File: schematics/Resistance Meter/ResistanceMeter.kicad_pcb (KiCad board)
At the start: 2 copper layers, 52.7 x 54.6 mm, 29 parts, among them J1 Conn_01x01_Female, J2 Conn_01x01_Female, J3 Conn_01x16_Female, J4 Conn_01x08_Male, J5 Conn_01x06_Male, J6 Conn_01x10_Male, J7 Conn_01x08_Male, Q1 IRF540N, Q2 IRF540N, SW1 SW_Push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

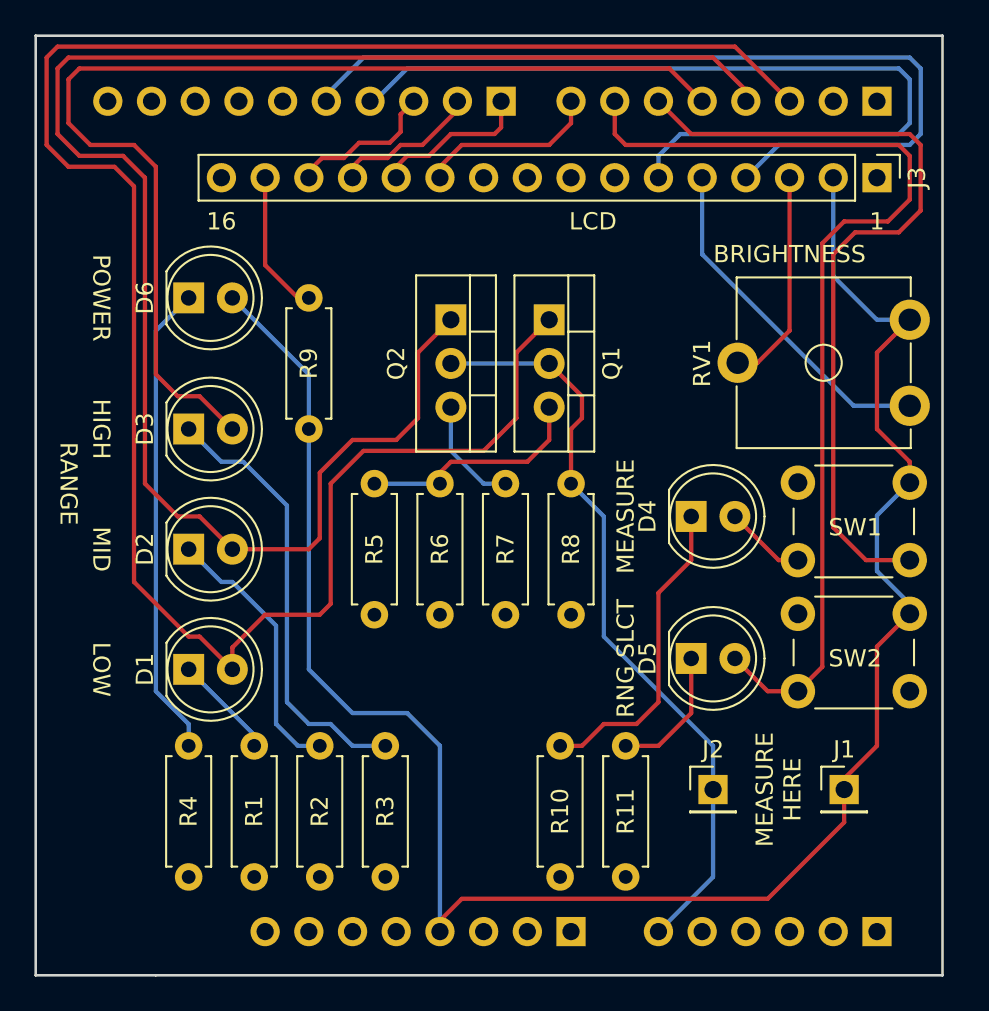
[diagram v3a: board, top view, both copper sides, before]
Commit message: Update to KiCad 5 from 4
- use KiCad's standard library Arduino shield symbol and footprint
- ground the second copper layer of the PCB (and consequently unground
the first copper layer of the PCB)
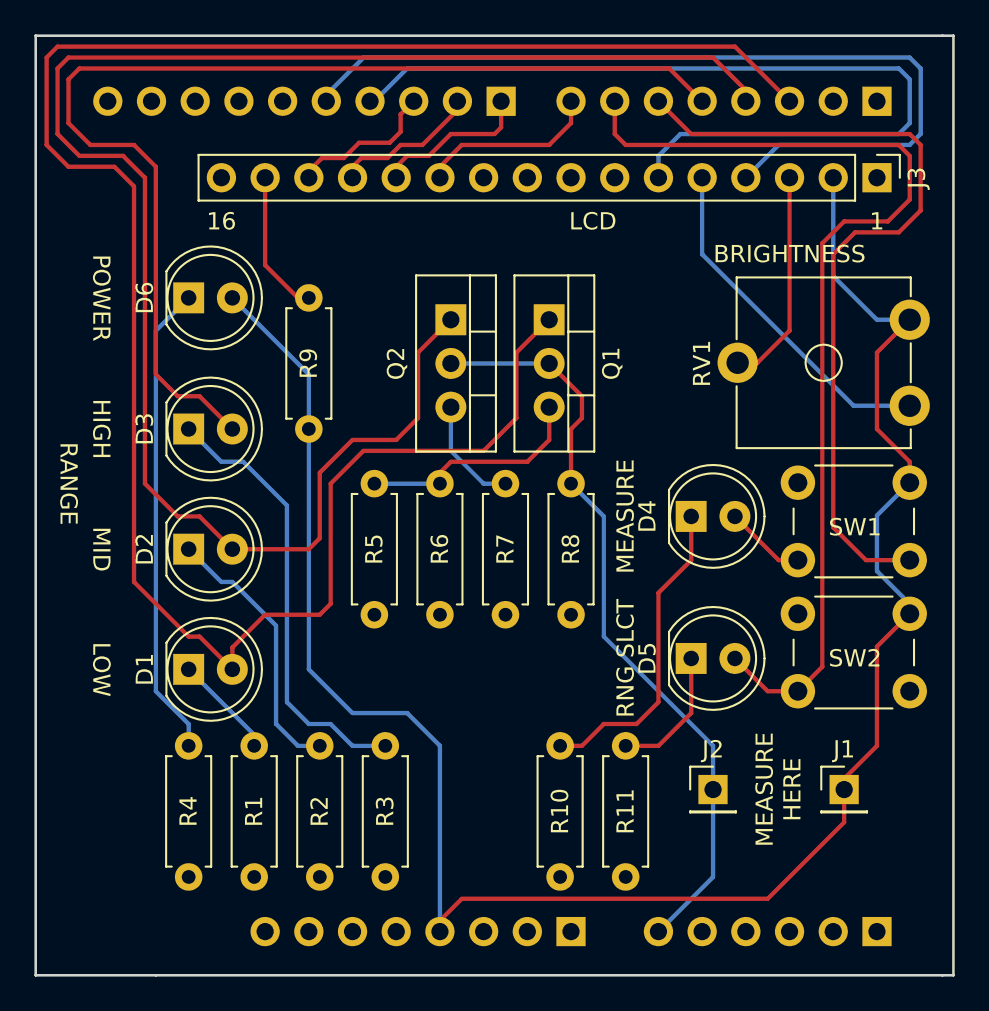
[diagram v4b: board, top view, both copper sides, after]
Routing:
- added copper zone on B.Cu, net Earth
- removed copper zone on F.Cu, net Earth
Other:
- board size 52.7 x 54.6 mm -> 53.3 x 54.6 mm
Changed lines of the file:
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@@
-(kicad_pcb (version 4) (host pcbnew 4.0.7-e2-6376~61~ubuntu18.04.1)
+(kicad_pcb (version 20171130) (host pcbnew 5.0.0-fee4fd1~65~ubuntu18.04.1)
   (general
-    (links 55)
-    (no_connects 4)
-    (area 128.194999 64.694999 181.050001 119.455001)
     (thickness 1.6)
-    (drawings 18)
+    (drawings 20)
     (tracks 207)
     (zones 0)
@@
     (visible_elements FFFFFF7F)
     (pcbplotparams
-      (layerselection 0x00030_80000001)
+      (layerselection 0x010f0_ffffffff)
       (usegerberextensions false)
+      (usegerberattributes false)
+      (usegerberadvancedattributes false)
+      (creategerberjobfile false)
       (excludeedgelayer true)
       (linewidth 0.100000)
@@
       (hpglpennumber 1)
       (hpglpenspeed 20)
-      (hpglpendiameter 15)
-      (hpglpenoverlay 2)
+      (hpglpendiameter 15.000000)
       (psnegative false)
       (psa4output false)
@@
       (outputformat 1)
       (mirror false)
-      (drillshape 1)
+      (drillshape 0)
       (scaleselection 1)
-      (outputdirectory ""))
+      (outputdirectory "gerber/"))
   )
   (net 0 "")
@@
       (net 45 "Net-(Q1-Pad3)"))
     (model ${KISYS3DMOD}/TO_SOT_Packages_THT.3dshapes/TO-220-3_Vertical.wrl
-      (at (xyz 0.1 0 0))
+      (offset (xyz 2.539999961853027 0 0))
       (scale (xyz 0.393701 0.393701 0.393701))
       (rotate (xyz 0 0 0))
@@
       (net 2 Earth))
     (model ${KISYS3DMOD}/Socket_Strips.3dshapes/Socket_Strip_Straight_1x16_Pitch2.54mm.wrl
-      (at (xyz 0 -0.75 0))
+      (offset (xyz 0 -19.04999971389771 0))
       (scale (xyz 1 1 1))
       (rotate (xyz 0 0 270))
@@
     (fp_line (start 1.8 -19.55) (end 1.8 1.8) (layer B.CrtYd) (width 0.05))
     (fp_line (start 1.8 1.8) (end -1.8 1.8) (layer B.CrtYd) (width 0.05))
-    (fp_text user %R (at 0 -8.89 360) (layer B.Fab)
+    (fp_text user %R (at 0 -8.89) (layer B.Fab)
       (effects (font (size 1 1) (thickness 0.15)) (justify mirror))
     )
@@
     (fp_line (start 1.8 -14.5) (end 1.8 1.8) (layer B.CrtYd) (width 0.05))
     (fp_line (start 1.8 1.8) (end -1.8 1.8) (layer B.CrtYd) (width 0.05))
-    (fp_text user %R (at 0 -6.35 360) (layer B.Fab)
+    (fp_text user %R (at 0 -6.35) (layer B.Fab)
       (effects (font (size 1 1) (thickness 0.15)) (justify mirror))
     )
@@
     (fp_line (start 1.8 -24.65) (end 1.8 1.8) (layer B.CrtYd) (width 0.05))
     (fp_line (start 1.8 1.8) (end -1.8 1.8) (layer B.CrtYd) (width 0.05))
-    (fp_text user %R (at 0 -11.43 360) (layer B.Fab)
+    (fp_text user %R (at 0 -11.43) (layer B.Fab)
       (effects (font (size 1 1) (thickness 0.15)) (justify mirror))
     )
@@
     (fp_line (start 1.8 -19.55) (end 1.8 1.8) (layer B.CrtYd) (width 0.05))
     (fp_line (start 1.8 1.8) (end -1.8 1.8) (layer B.CrtYd) (width 0.05))
-    (fp_text user %R (at 0 -8.89 360) (layer B.Fab)
+    (fp_text user %R (at 0 -8.89) (layer B.Fab)
       (effects (font (size 1 1) (thickness 0.15)) (justify mirror))
     )
@@
       (net 46 "Net-(Q2-Pad3)"))
     (model ${KISYS3DMOD}/TO_SOT_Packages_THT.3dshapes/TO-220-3_Vertical.wrl
-      (at (xyz 0.1 0 0))
+      (offset (xyz 2.539999961853027 0 0))
       (scale (xyz 0.393701 0.393701 0.393701))
       (rotate (xyz 0 0 0))
@@
       (net 7 /b5))
     (model ${KISYS3DMOD}/Buttons_Switches_THT.3dshapes/SW_PUSH_6mm_h4.3mm.wrl
-      (at (xyz 0.005 0 0))
+      (offset (xyz 0.1269999980926514 0 0))
       (scale (xyz 0.3937 0.3937 0.3937))
       (rotate (xyz 0 0 0))
@@
       (net 8 /b6))
     (model ${KISYS3DMOD}/Buttons_Switches_THT.3dshapes/SW_PUSH_6mm_h4.3mm.wrl
-      (at (xyz 0.005 0 0))
+      (offset (xyz 0.1269999980926514 0 0))
       (scale (xyz 0.3937 0.3937 0.3937))
       (rotate (xyz 0 0 0))
     )
   )
+  (gr_line (start 181.61 119.38) (end 180.975 119.38) (layer Edge.Cuts) (width 0.15))
+  (gr_line (start 180.975 64.77) (end 181.61 64.77) (layer Edge.Cuts) (width 0.15))
   (gr_text "DESIGNED BY PETAR NIKOLOV" (at 131.445 90.17 270) (layer B.SilkS)
     (effects (font (size 1 1) (thickness 0.15)) (justify mirror))
@@
   (gr_line (start 135.255 119.38) (end 128.27 119.38) (angle 90) (layer Edge.Cuts) (width 0.15))
   (gr_line (start 180.975 119.38) (end 135.255 119.38) (angle 90) (layer Edge.Cuts) (width 0.15))
-  (gr_line (start 180.975 64.77) (end 180.975 119.38) (angle 90) (layer Edge.Cuts) (width 0.15))
+  (gr_line (start 181.61 64.77) (end 181.61 119.38) (angle 90) (layer Edge.Cuts) (width 0.15))
   (segment (start 158.115 83.82) (end 152.4 83.82) (width 0.25) (layer B.Cu) (net 1))
   (segment (start 159.385 90.805) (end 159.385 87.63) (width 0.25) (layer F.Cu) (net 1))
@@
   (segment (start 161.29 99.695) (end 161.29 92.71) (width 0.25) (layer B.Cu) (net 1))
   (segment (start 167.64 106.045) (end 161.29 99.695) (width 0.25) (layer B.Cu) (net 1))
-  (segment (start 179.07 86.28) (end 175.815 86.28) (width 0.25) (layer B.Cu) (net 2))
-  (segment (start 167.005 77.47) (end 167.005 73.025) (width 0.25) (layer B.Cu) (net 2))
-  (segment (start 175.815 86.28) (end 167.005 77.47) (width 0.25) (layer B.Cu) (net 2))
+  (segment (start 179.07 86.28) (end 175.815 86.28) (width 0.25) (layer B.Cu) (net 2) (status 1000000))
+  (segment (start 167.005 77.47) (end 167.005 73.025) (width 0.25) (layer B.Cu) (net 2) (status 1000000))
+  (segment (start 175.815 86.28) (end 167.005 77.47) (width 0.25) (layer B.Cu) (net 2) (status 1000000))
   (segment (start 144.145 87.63) (end 144.145 101.6) (width 0.25) (layer B.Cu) (net 3))
   (segment (start 151.765 106.045) (end 151.765 116.84) (width 0.25) (layer B.Cu) (net 3))
@@
   (segment (start 152.4 88.9) (end 152.4 86.36) (width 0.25) (layer B.Cu) (net 46))
   (segment (start 154.305 90.805) (end 152.4 88.9) (width 0.25) (layer B.Cu) (net 46))
-  (zone (net 2) (net_name Earth) (layer F.Cu) (hatch edge 0.508)
+  (zone (net 2) (net_name Earth) (layer B.Cu) (hatch edge 0.508)
     (connect_pads (clearance 0.508))
     (min_thickness 0.254)
@@
     (polygon
       (pts
-        (xy 180.975 119.38) (xy 128.27 119.38) (xy 128.27 64.77) (xy 180.975 64.77)
+        (xy 181.61 64.77) (xy 181.61 119.38) (xy 128.27 119.38) (xy 128.27 64.77)
       )
     )

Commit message: Revise the project's PCB design
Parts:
- removed J2: Conn_01x01_Female, Socket_Strips:Socket_Strip_Straight_1x01_Pitch2.54mm
- removed J3: Conn_01x16_Female, Socket_Strips:Socket_Strip_Straight_1x16_Pitch2.54mm
- removed J4, J7: Conn_01x08_Male, Pin_Headers:Pin_Header_Straight_1x08_Pitch2.54mm
- removed J5: Conn_01x06_Male, Pin_Headers:Pin_Header_Straight_1x06_Pitch2.54mm
- removed J6: Conn_01x10_Male, Pin_Headers:Pin_Header_Straight_1x10_Pitch2.54mm
- removed R11: 220, Resistors_THT:R_Axial_DIN0207_L6.3mm_D2.5mm_P7.62mm_Horizontal
- added A1: Arduino_UNO_R3, Modules:Arduino_UNO_R3, B.Cu at (136.5, 109.9)
- added DS1: NDS1602A, Displays:WC1602A, F.Cu at (167.0, 66.7)
- added Q3: IRF520, IRF520:TO220BV, F.Cu at (153.7, 75.6)
- J1: value Conn_01x01_Female -> Conn_01x02_Male; footprint Socket_Strips:Socket_Strip_Straight_1x01_Pitch2.54mm -> Pin_Headers:Pin_Header_Straight_1x02_Pitch2.54mm
- Q1, Q2: value IRF540N -> IRF520; footprint TO_SOT_Packages_THT:TO-220-3_Vertical -> IRF520:TO220BV
- R1, R2, R3, R4, R5, R6, R9: value 220 -> 220R
- R10: value 220 -> 10M
- R7: value 10k -> 100R
- R8: value 10M -> 10k
- moved D5 46.7 mm to (128.9, 73.0)
- moved D4 39.6 mm to (128.9, 80.0)
- moved D1 26.3 mm to (158.1, 85.7)
- moved R9 24.3 mm to (128.3, 98.4)
- moved R10 23.5 mm to (151.1, 83.8)
- moved R6 21.7 mm to (131.4, 98.4)
- moved D2 21.0 mm to (158.1, 92.7)
- moved R7 19.7 mm to (137.2, 83.8)
- moved Q1 19.3 mm to (139.7, 75.6)
- moved R1 17.7 mm to (157.5, 99.7)
- moved R2 17.1 mm to (160.7, 99.7)
- moved R8 16.8 mm to (144.1, 83.8)
- moved D6 16.2 mm to (128.9, 94.0)
- moved R3 15.9 mm to (134.6, 98.4)
- moved R5 10.3 mm to (141.0, 98.4)
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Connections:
- net Earth renamed GND
- D1 pad 2: /b2 -> Net-(A1-Pad20)
- D2 pad 2: /b3 -> Net-(A1-Pad21)
- D3 pad 2: /b4 -> Net-(A1-Pad19)
- D4 pad 2: /b5 -> Net-(A1-Pad18)
- D5 pad 2: /b6 -> Net-(A1-Pad17)
- J1 pad 1: +5V -> /ANALOG_INPUT
- R10 pad 1: Net-(D4-Pad1) -> Net-(Q3-PadS)
- R4 pad 1: Net-(D6-Pad1) -> Net-(D4-Pad1)
- R5 pad 1: Net-(Q1-Pad3) -> Net-(D5-Pad1)
- R6 pad 1: Net-(Q1-Pad3) -> Net-(D6-Pad1)
- R7 pad 1: Net-(Q2-Pad3) -> Net-(Q1-PadS)
- R8 pad 1: /ANALOG_INPUT -> Net-(Q2-PadS)
- R9 pad 1: /a15 -> Net-(DS1-Pad15)
- RV1 pad 2: /a3 -> Net-(DS1-Pad3)
- SW1 pad 1: /b5 -> Net-(A1-Pad20)
- SW2 pad 1: /b6 -> Net-(A1-Pad21)
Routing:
- net /b2: track 120.6 -> 0.00 mm
- net +5V: track 115.3 -> 0.00 mm
- net /b3: track 98.8 -> 0.00 mm
- net Net-(A1-Pad19): track 0.00 -> 82.6 mm
- net Net-(A1-Pad18): track 0.00 -> 67.8 mm
- net /b4: track 64.4 -> 0.00 mm
- net Net-(A1-Pad21): track 0.00 -> 64.2 mm
- net /b6: track 59.3 -> 0.00 mm
- net /b5: track 52.8 -> 0.00 mm
- net /a6: track 51.6 -> 0.00 mm
- net /a4: track 51.1 -> 0.00 mm
- net Net-(A1-Pad20): track 0.00 -> 49.9 mm
- net Net-(A1-Pad17): track 0.00 -> 46.8 mm
- net Net-(D5-Pad1): track 7.77 -> 44.6 mm
- net Net-(DS1-Pad15): track 0.00 -> 36.3 mm
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- added copper zone on F.Cu, net +5V
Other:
- board size 53.3 x 54.6 mm -> 54.6 x 54.6 mm
- board text added: "Arduino Uno R3"
- board text removed: "LCD"
- board text removed: "RANGE"
